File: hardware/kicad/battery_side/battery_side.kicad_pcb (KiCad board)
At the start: 2 copper layers, 60 x 40 mm, 45 parts

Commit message: hardware: CP3 iter 8 — Finding 02 (REF**) fix + D11 (engineer-readable docs)
Two updates this iter.

1) Finding 02 fix — refdes on placed footprints

KiCad 10 stores Reference/Value as fp.properties dict entries;
silkscreen FpText uses ${REFERENCE} substitution. The legacy
KiCad 6/7 typed-FpText override was a no-op on the cached
KiCad 10 footprints.

Fix in build_pcbs.py _place_footprint / _add_mounting_holes /
build_smoke: set fp.properties["Reference"]/["Value"] per instance
(keeping the typed-FpText path as a fallback for legacy libs).

Verification:
  grep -cF '(property "Reference"' battery_side.kicad_pcb       → 45
  ... | sort -u | wc -l                                          → 45

41 components (J1...MOD1) + 4 mounting holes (H1-H4) all show
unique refdes in renders. DRC still 0 errors.

2) D11 — engineer-readable documentation rule

User reviewed CP2 schematic PDFs and pushed back on readability
(overlapping symbols, label-only connections, blank title block,
no functional grouping).

New project rule:
- hardware/layout/decisions.md §D11 lists seven concrete acceptance
  criteria (no overlap, real wires in clusters, populated title
  block, signal flow, legible at 100% zoom, consistent rails,
  refdes on renders).
- hardware/reviews/DESIGNER.md §0 flags readability as a first-class
  deliverable equal to correctness.
- Each CP success-criteria section now includes a D11 checkbox.

CP2 schematic PDFs currently violate D11. Remediation is staged as
a discrete "schematic-cleanup" checkpoint between CP3 close and
CP4 open, on a branch off main, with the safety belt that ERC must
remain 0/0 and netlist topology byte-identical to current outputs.
That CP does not block CP3.

Top + bottom renders for battery_side regenerated showing real
refdes (D11 criterion #7 now satisfied for this PCB).

SEMAPHORE -> codex_turn iter 9.

Co-Authored-By: Claude Opus 4.7 (1M context) <noreply@anthropic.com>
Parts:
- removed REF**: BatteryHolder_Keystone_1057_1x2032, volthium:BatteryHolder_Keystone_1057_1x2032
- removed REF**: C_0805_2012Metric, volthium:C_0805_2012Metric
- removed REF**: C_0402_1005Metric, volthium:C_0402_1005Metric
- removed REF** (x6): C_0603_1608Metric, volthium:C_0603_1608Metric
- removed REF** (x3): D_SMA, volthium:D_SMA
- removed REF**: Fuseholder_Clip-5x20mm_Bel_FC-203-22_Lateral_P17.80x5.00mm_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, volthium:Fuseholder_Clip-5x20mm_Bel_FC-203-22_Lateral_P17.80x5.00mm_D1.17mm_Horizontal
- removed REF**: TerminalBlock_Phoenix_MKDS-1,5-2-5.08_1x02_P5.08mm_Horizont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, volthium:TerminalBlock_Phoenix_MKDS-1,5-2-5.08_1x02_P5.08mm_Horizontal
- removed REF**: RJ45_Amphenol_RJHSE5380, volthium:RJ45_Amphenol_RJHSE5380
- removed REF** (x2): PinHeader_1x04_P2.54mm_Vertical, volthium:PinHeader_1x04_P2.54mm_Vertical
- removed REF**: SW_PUSH_6mm, volthium:SW_PUSH_6mm
- removed REF**: L_0805_2012Metric, volthium:L_0805_2012Metric
- removed REF**: ESP32-S3-WROOM-1, volthium:ESP32-S3-WROOM-1
- removed REF** (x2): SOT-23, volthium:SOT-23
- removed REF** (x11): R_0805_2012Metric, volthium:R_0805_2012Metric
- removed REF** (x4): C_1210_3225Metric, volthium:C_1210_3225Metric
- removed REF**: SOIC-16W_7.5x10.3mm_P1.27mm, volthium:SOIC-16W_7.5x10.3mm_P1.27mm
- removed REF**: SOT-23-6, volthium:SOT-23-6
- removed REF**: Converter_DCDC_RECOM_R-78E-0.5_THT, volthium:Converter_DCDC_RECOM_R-78E-0.5_THT
- removed REF**: SOIC-8_3.9x4.9mm_P1.27mm, volthium:SOIC-8_3.9x4.9mm_P1.27mm
- removed REF** (x4): MountingHole_3.2mm_M3_DIN965, volthium:MountingHole_3.2mm_M3_DIN965
- added BAT1: CR2032, volthium:BatteryHolder_Keystone_1057_1x2032, F.Cu at (105.0, 40.0)
- added BTN1: OVERRIDE, volthium:SW_PUSH_6mm, F.Cu at (105.0, 55.0)
- added C1: 22uF/25V, volthium:C_1210_3225Metric, F.Cu at (42.0, 11.5)
- added C10: 100nF, volthium:C_0603_1608Metric, F.Cu at (90.0, 85.0)
- added C11: 100nF, volthium:C_0603_1608Metric, F.Cu at (105.0, 85.0)
- added C2: 22uF/25V, volthium:C_1210_3225Metric, F.Cu at (46.5, 11.5)
- added C3: 22uF/35V, volthium:C_1210_3225Metric, F.Cu at (51.0, 7.50)
- added C4: 22uF/25V, volthium:C_1210_3225Metric, F.Cu at (51.0, 11.5)
- added C5: 100nF, volthium:C_0603_1608Metric, B.Cu at (10.0, 21.0)
- added C6: 10uF, volthium:C_0805_2012Metric, F.Cu at (90.0, 25.0)
- added C7: 100nF, volthium:C_0402_1005Metric, F.Cu at (105.0, 25.0)
- added C8: 1uF, volthium:C_0603_1608Metric, F.Cu at (120.0, 25.0)
- added C9: 100nF, volthium:C_0603_1608Metric, F.Cu at (90.0, 55.0)
- added C_BST: 100nF, volthium:C_0603_1608Metric, F.Cu at (43.5, 4.00)
- added D1: SS24, volthium:D_SMA, F.Cu at (37.0, 7.50)
- added F1: 1A 5x20, volthium:Fuseholder_Clip-5x20mm_Bel_FC-203-22_Lateral_P17.80x5.00mm_D1.17mm_Horizontal, F.Cu at (24.5, 8.50)
- added H1: MountingHole_3.2mm, volthium:MountingHole_3.2mm_M3_DIN965, F.Cu at (3.00, 3.00)
- added H2: MountingHole_3.2mm, volthium:MountingHole_3.2mm_M3_DIN965, F.Cu at (57.0, 3.00)
- added H3: MountingHole_3.2mm, volthium:MountingHole_3.2mm_M3_DIN965, F.Cu at (3.00, 37.0)
- added H4: MountingHole_3.2mm, volthium:MountingHole_3.2mm_M3_DIN965, F.Cu at (57.0, 37.0)
- added J1: Conn_01x02, volthium:TerminalBlock_Phoenix_MKDS-1,5-2-5.08_1x02_P5.08mm_Horizontal, F.Cu at (9.00, 8.50)
- added J2: RJ45, volthium:RJ45_Amphenol_RJHSE5380, F.Cu at (105.0, 100.0)
- added J3: USB-OTG, volthium:PinHeader_1x04_P2.54mm_Vertical, F.Cu at (120.0, 100.0)
- added J5: UART-DBG, volthium:PinHeader_1x04_P2.54mm_Vertical, F.Cu at (75.0, 115.0)
- added L1: 2.2uH, volthium:L_0805_2012Metric, F.Cu at (46.5, 7.50)
- added MOD1: ESP32-S3-WROOM-1-N16R8, volthium:ESP32-S3-WROOM-1, F.Cu at (75.0, 25.0)
- added Q1: AO3401A, volthium:SOT-23, F.Cu at (75.0, 10.0)
- added Q2: AO3400A, volthium:SOT-23, F.Cu at (90.0, 10.0)
- added R10: 120, volthium:R_0805_2012Metric, F.Cu at (90.0, 70.0)
- added R11: 680, volthium:R_0805_2012Metric, F.Cu at (105.0, 70.0)
- added R12: 680, volthium:R_0805_2012Metric, F.Cu at (120.0, 70.0)
- added R13: 1M, volthium:R_0805_2012Metric, F.Cu at (120.0, 55.0)
- added R3: 100k, volthium:R_0805_2012Metric, F.Cu at (105.0, 10.0)
- added R4: 100k, volthium:R_0805_2012Metric, F.Cu at (120.0, 10.0)
- added R5: 1M, volthium:R_0805_2012Metric, B.Cu at (10.0, 16.0)
- added R6: 110k, volthium:R_0805_2012Metric, B.Cu at (10.0, 18.5)
- added R7: 10k, volthium:R_0805_2012Metric, F.Cu at (75.0, 40.0)
- added R8: 4.7k, volthium:R_0805_2012Metric, F.Cu at (120.0, 40.0)
- added R9: 4.7k, volthium:R_0805_2012Metric, F.Cu at (75.0, 55.0)
- added RTC1: DS3231SN#, volthium:SOIC-16W_7.5x10.3mm_P1.27mm, F.Cu at (90.0, 40.0)
- added TVS1: SMAJ30CA, volthium:D_SMA, F.Cu at (37.0, 10.5)
- added TVS2: SMAJ12CA, volthium:D_SMA, F.Cu at (75.0, 85.0)
- added U1: TPS62933FDRLR, volthium:SOT-23-6, F.Cu at (42.0, 7.50)
- added U2: R-78E12-1.0, volthium:Converter_DCDC_RECOM_R-78E-0.5_THT, F.Cu at (54.0, 18.0)
- added U3: SN65HVD3082E, volthium:SOIC-8_3.9x4.9mm_P1.27mm, F.Cu at (75.0, 70.0)

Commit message: hardware: CP3 iter 10 — hard-cut + ESP32 module + MCU bypass
9 components moved from parked to on-board:

  Q1/Q2/R3/R4   hard-cut pair (AO3401A P-FET, AO3400A N-FET, gate R)
                left of MOD1 at x=16-20, y=17-22
  MOD1          ESP32-S3-WROOM-1 anchor at (28.0, 16.5)
                module body x=19-37, y=3.75-29.25
                pin 2 (3V3) at absolute (19.25, 12.51)
  C6/C7/C8      MCU bypass row on B.Cu directly under pin 2
                short via stitches keep decoupling loop small
  R7            10kΩ EN pullup on B.Cu next to bypass

DRC: 0 errors (overrides in battery_side.kicad_pro for CP3-phase
noise: unconnected_items / courtyards / silk / drill / edge).

Top + bottom renders regenerated; parked cluster shrunk from 28 to
19 components.

What's still parked for iter 12:
  RTC1, BAT1, R8, R9, C9        RTC + backup cell
  BTN1, R13                     override button
  U3, R10-R12, TVS2, C10        RS-485
  C11-C14                       misc decoupling
  J2, J3, J5                    RJ45 + dev headers

iter 12 also covers: antenna keepout zone, net classes per CP1
§11.3, final battery-side renders. Display-side placement follows
at iter 14.

SEMAPHORE -> codex_turn iter 11.

Co-Authored-By: Claude Opus 4.7 (1M context) <noreply@anthropic.com>
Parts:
- C6, C7, C8, R7: moved to B.Cu
- moved R4 100.2 mm to (20.0, 17.0)
- moved C8 98.7 mm to (22.0, 13.5)
- moved C7 85.8 mm to (20.0, 13.5)
- moved R3 85.8 mm to (20.0, 21.5)
- moved Q2 74.9 mm to (16.0, 21.5)
- moved C6 72.9 mm to (18.0, 13.5)
- moved J5 63.6 mm to (120.0, 70.0)
- moved R9 63.6 mm to (120.0, 10.0)
- moved TVS2 63.6 mm to (120.0, 40.0)
- moved U3 63.6 mm to (120.0, 25.0)
- moved R7 60.2 mm to (20.0, 15.5)
- moved Q1 59.4 mm to (16.0, 17.0)
- moved MOD1 47.8 mm to (28.0, 16.5)
- moved BAT1 33.5 mm to (90.0, 10.0)
- moved BTN1 33.5 mm to (90.0, 25.0)
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
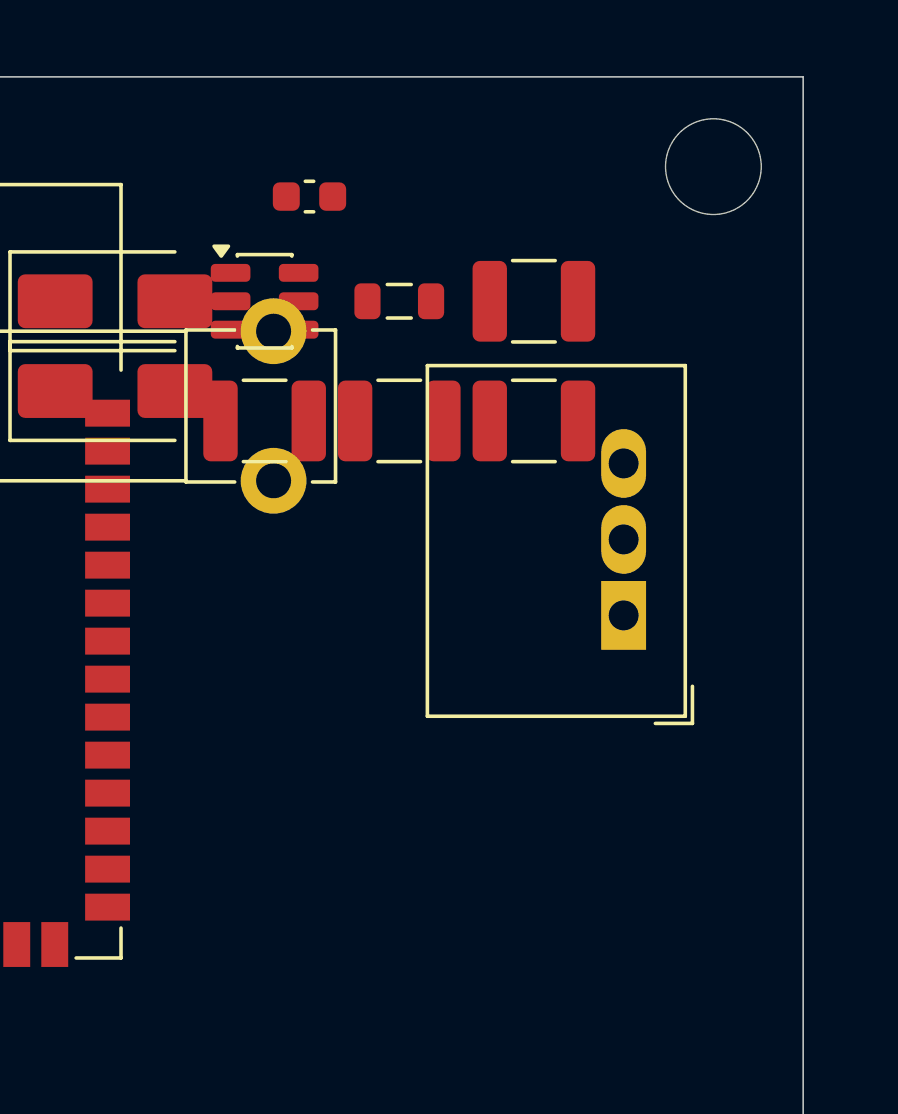
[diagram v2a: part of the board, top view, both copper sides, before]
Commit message: hardware: CP3 iter 12 — Finding 03 (U1/F1 hole_clearance) fixed
Codex's Finding 03 was correct. My earlier "0 errors" was misleading
because I had been invoking kicad-cli pcb drc from the repo root,
which does not pick up the project's .kicad_pro severity overrides.
Running DRC from hardware/kicad/battery_side/ surfaces the real
hole_clearance error.

Root cause: the Bel FC-203-22 fuse-clip footprint has 4 THT pads in
a 2x2 grid spanning x=24.5-42.3, y=8.5-13.5 (1.17mm drill). The U1
cluster (TPS62933 + bulk caps) at x=42-51 overlapped F1's right
column of THT pads in copper-edge space.

Geometric fix (no severity suppression added; hole_clearance
remains at default 'error'):

  U1     -> (45.0, 7.5)         was (40.5, 7.5)
  C1     -> (45.0, 11.5)
  C_BST  -> (46.5, 4.0)
  L1     -> (49.0, 7.5)
  C2     -> (49.0, 11.5)
  C3     -> (52.5, 7.5)
  C4     -> (52.5, 11.5)
  U2     -> (54.0, 25.0)        moved down from (54, 18) to clear C4

Verification (matching Codex's invocation):
  cd hardware/kicad/battery_side
  kicad-cli pcb drc --severity-error battery_side.kicad_pcb
  -> Found 0 violations, 0 unconnected items, 0 footprint errors

Workflow lesson: DRC must be invoked from the project directory in
this repo so .kicad_pro overrides apply. Will thread this through
build_pcbs.py / a small check.sh in iter 14.

Top + bottom renders regenerated.

SEMAPHORE -> codex_turn iter 13.

Co-Authored-By: Claude Opus 4.7 (1M context) <noreply@anthropic.com>
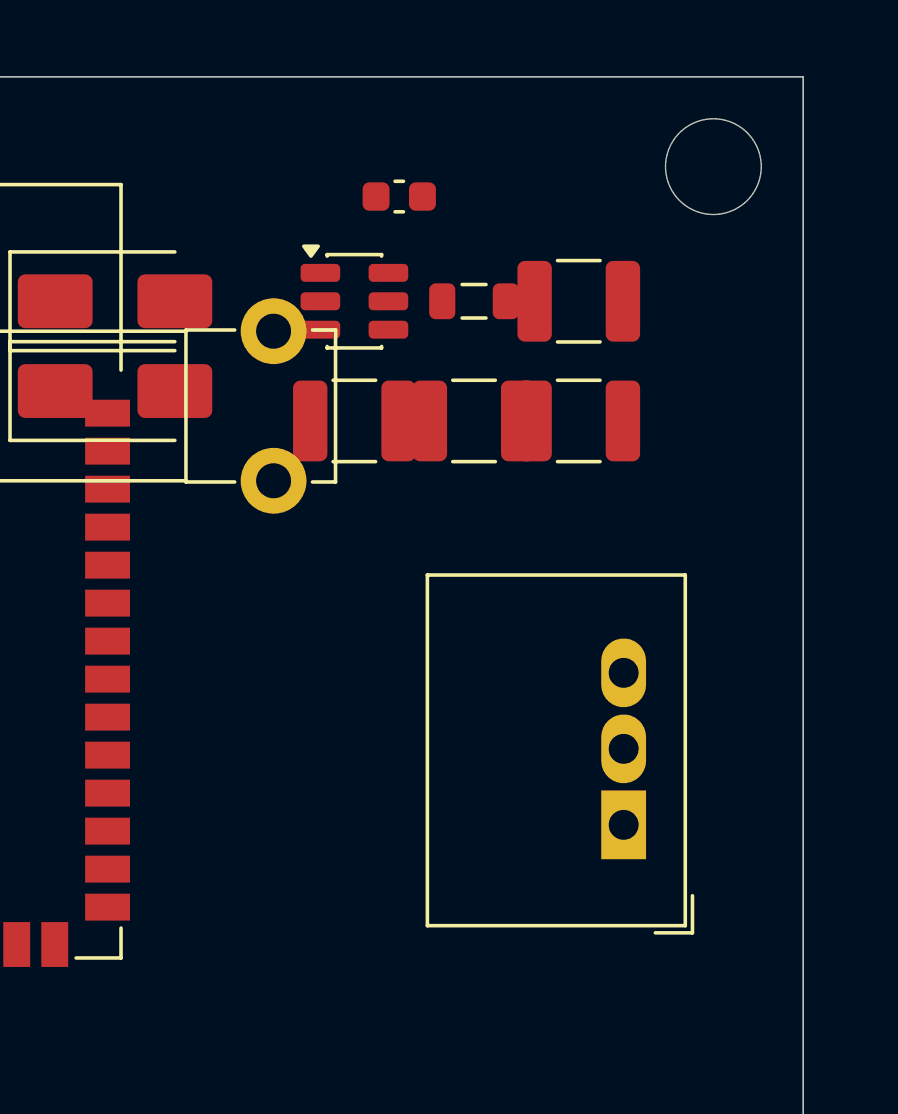
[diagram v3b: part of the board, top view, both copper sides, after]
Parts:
- moved U2 7.00 mm to (54.0, 25.0)
- moved C1 3.00 mm to (45.0, 11.5)
- moved C_BST 3.00 mm to (46.5, 4.00)
- moved U1 3.00 mm to (45.0, 7.50)
- moved C2 2.50 mm to (49.0, 11.5)
- moved L1 2.50 mm to (49.0, 7.50)
- moved C3 1.50 mm to (52.5, 7.50)
- moved C4 1.50 mm to (52.5, 11.5)
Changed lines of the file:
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@@
   )
   (footprint "volthium:C_1210_3225Metric" (version 20260206) (generator kicad-footprint-generator) (layer "F.Cu")
-    (at 42.0 11.5 0)
+    (at 45.0 11.5 0)
     (descr "Capacitor SMD 1210 (3225 Metric), square (rectangular) end terminal, IPC-7351 nominal, (Body size source: IPC-SM-782 page 76, https://www.pcb-3d.com/wordpress/wp-content/uploads/ipc-sm-782a_amendment_1_and_2.pdf)")
     (tags "capacitor")
@@
   )
   (footprint "volthium:C_1210_3225Metric" (version 20260206) (generator kicad-footprint-generator) (layer "F.Cu")
-    (at 46.5 11.5 0)
+    (at 49.0 11.5 0)
     (descr "Capacitor SMD 1210 (3225 Metric), square (rectangular) end terminal, IPC-7351 nominal, (Body size source: IPC-SM-782 page 76, https://www.pcb-3d.com/wordpress/wp-content/uploads/ipc-sm-782a_amendment_1_and_2.pdf)")
     (tags "capacitor")
@@
   )
   (footprint "volthium:C_1210_3225Metric" (version 20260206) (generator kicad-footprint-generator) (layer "F.Cu")
-    (at 51.0 7.5 0)
+    (at 52.5 7.5 0)
     (descr "Capacitor SMD 1210 (3225 Metric), square (rectangular) end terminal, IPC-7351 nominal, (Body size source: IPC-SM-782 page 76, https://www.pcb-3d.com/wordpress/wp-content/uploads/ipc-sm-782a_amendment_1_and_2.pdf)")
     (tags "capacitor")
@@
   )
   (footprint "volthium:C_1210_3225Metric" (version 20260206) (generator kicad-footprint-generator) (layer "F.Cu")
-    (at 51.0 11.5 0)
+    (at 52.5 11.5 0)
     (descr "Capacitor SMD 1210 (3225 Metric), square (rectangular) end terminal, IPC-7351 nominal, (Body size source: IPC-SM-782 page 76, https://www.pcb-3d.com/wordpress/wp-content/uploads/ipc-sm-782a_amendment_1_and_2.pdf)")
     (tags "capacitor")
@@
   )
   (footprint "volthium:C_0603_1608Metric" (version 20260206) (generator kicad-footprint-generator) (layer "F.Cu")
-    (at 43.5 4.0 0)
+    (at 46.5 4.0 0)
     (descr "Capacitor SMD 0603 (1608 Metric), square (rectangular) end terminal, IPC-7351 nominal, (Body size source: IPC-SM-782 page 76, https://www.pcb-3d.com/wordpress/wp-content/uploads/ipc-sm-782a_amendment_1_and_2.pdf)")
     (tags "capacitor")
@@
   )
   (footprint "volthium:L_0805_2012Metric" (version 20260206) (generator kicad-footprint-generator) (layer "F.Cu")
-    (at 46.5 7.5 0)
+    (at 49.0 7.5 0)
     (descr "Inductor SMD 0805 (2012 Metric), square (rectangular) end terminal, IPC-7351 nominal, (Body size source: IPC-SM-782 page 80, https://www.pcb-3d.com/wordpress/wp-content/uploads/ipc-sm-782a_amendment_1_and_2.pdf)")
     (tags "inductor")
@@
   )
   (footprint "volthium:SOT-23-6" (version 20260206) (generator kicad-footprint-generator) (layer "F.Cu")
-    (at 42.0 7.5 0)
+    (at 45.0 7.5 0)
     (descr "SOT, 6 Pin (JEDEC MO-178 Var AB https://www.jedec.org/document_search?search_api_views_fulltext=MO-178)")
     (tags "SOT TO_SOT_SMD")
@@
   )
   (footprint "volthium:Converter_DCDC_RECOM_R-78E-0.5_THT" (version 20260206) (generator kicad-footprint-generator) (layer "F.Cu")
-    (at 54.0 18.0 90)
+    (at 54.0 25.0 90)
     (descr "DCDC-Converter, RECOM, RECOM_R-78E-0.5, SIP-3, pitch 2.54mm, package size 11.6x8.5x10.4mm^3, https://www.recom-power.com/pdf/Innoline/R-78Exx-0.5.pdf")
     (tags "dc-dc recom buck sip-3 pitch 2.54mm")
